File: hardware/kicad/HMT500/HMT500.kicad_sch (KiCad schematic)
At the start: 0 parts

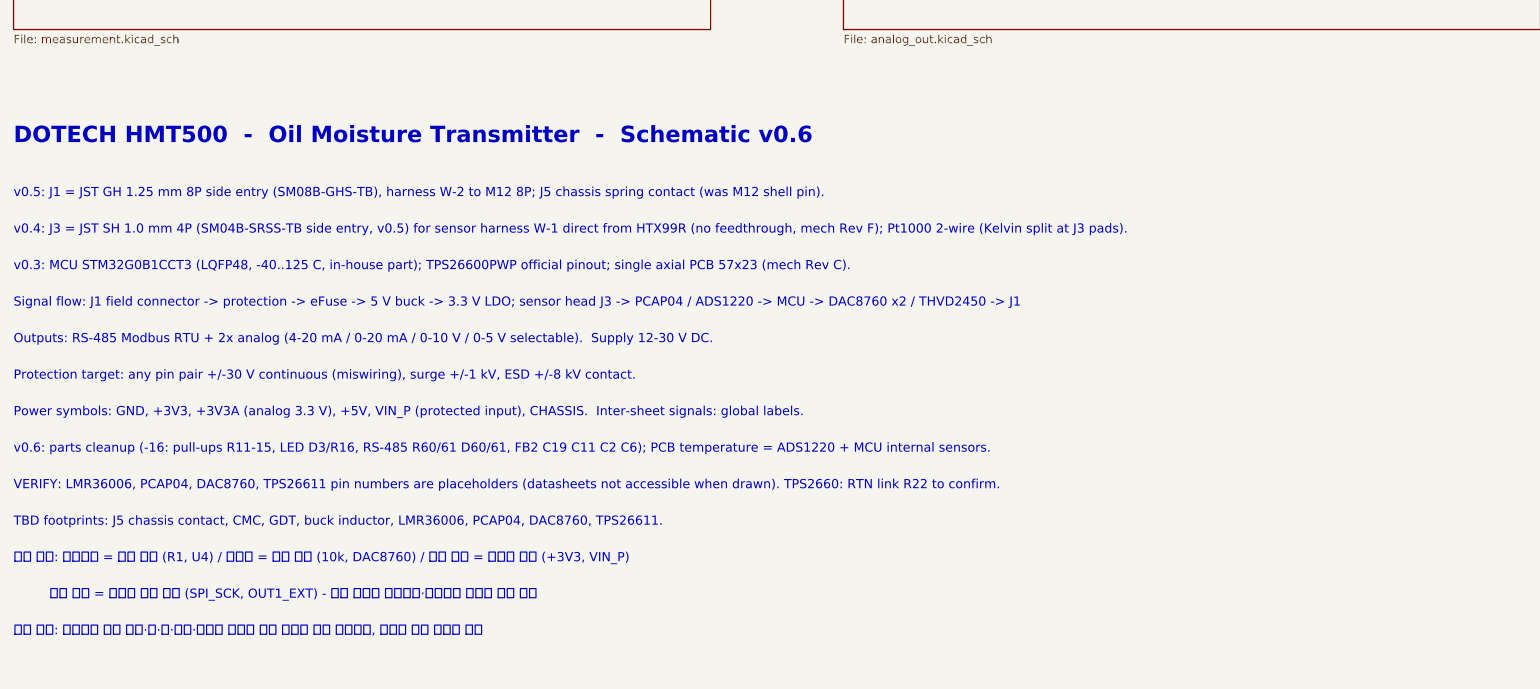
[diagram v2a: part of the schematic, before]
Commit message: Schematic v0.7: DAC8760 real pinout, OPA197 +VSENSE buffer, ISET-R, SPI2 daisy chain
- DAC8760 symbol from datasheet SBAS528D (HTSSOP-24 PWP + EP), same as
  VibrationSensor IVS320; placeholder pins removed, VERIFY flag dropped
- +VSENSE via OPA197 unity-gain follower (U12/U13) of the terminal voltage;
  R31/R41 10k kept as buffer input protection; C45/C55 V+ bypass
- External ISET-R 15k 0.1% 25 ppm (R32/R42)
- DACs on dedicated SPI2 (PB13/14/15) daisy chain with common DAC_LATCH
  (PB10); R33 100k pull-down on DAC_DAISY; ALARM -> PB11/PB3, PWR_FLT -> PB4
- Output protection unification (TPS26611 vs passive) left on hold
- Parts list, circuit-design doc, decision log #24 updated; netlist 70/70, 0 errors

Co-Authored-By: Claude Opus 5.5 <noreply@anthropic.com>
Claude-Session: https://claude.ai/code/session_01JA2o8uJsqp9Vzsg4b665ev
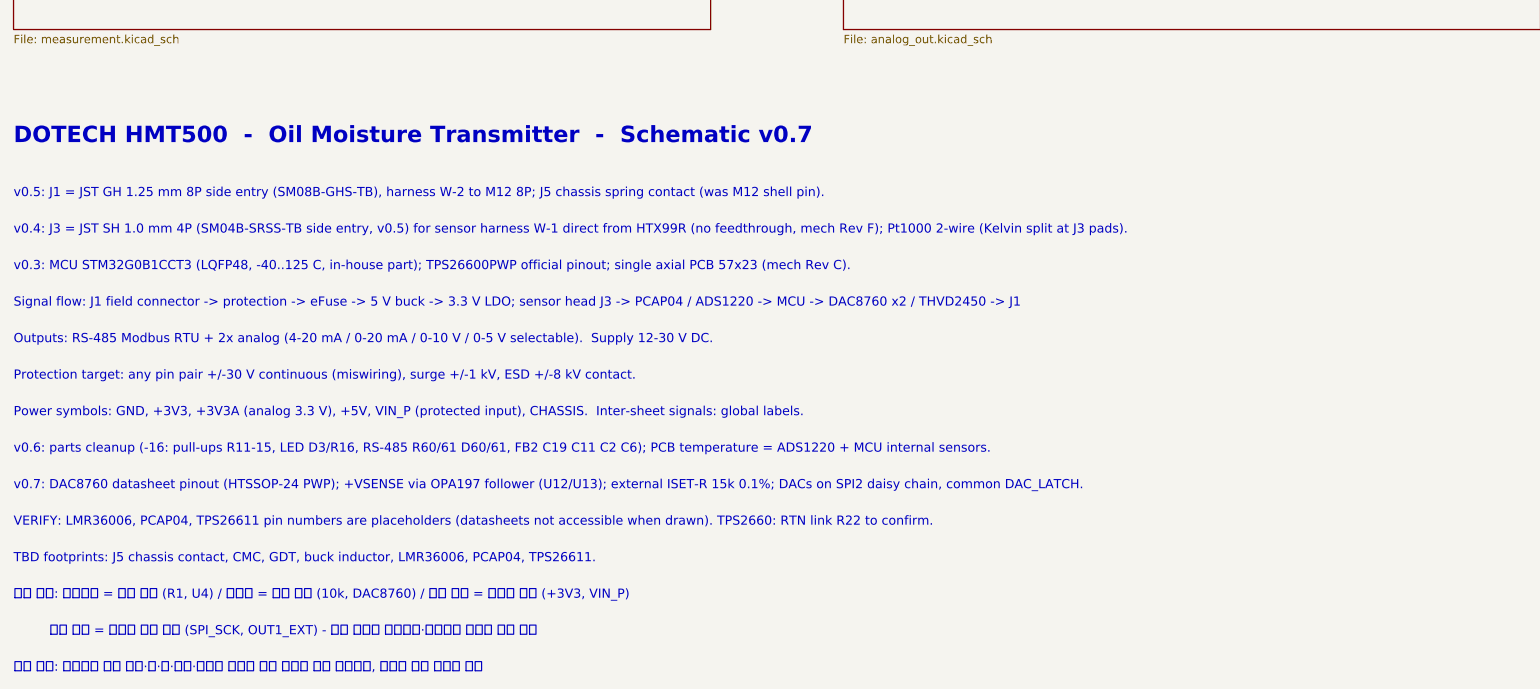
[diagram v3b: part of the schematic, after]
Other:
- note added: "DOTECH HMT500 - Oil Moisture Transmitter - Schematic v0.7"
- note added: "TBD footprints: J5 chassis contact, CMC, GDT, buck inductor, LMR36006, PCAP04, TPS26611."
- note added: "VERIFY: LMR36006, PCAP04, TPS26611 pin numbers are placeholders (datasheets not accessible when drawn). TPS2660: RTN link R22 to confirm."
- note added: "v0.7: DAC8760 datasheet pinout (HTSSOP-24 PWP); +VSENSE via OPA197 follower (U12/U13); external ISET-R 15k 0.1%; DACs on SPI2 daisy chain, common DAC_LATCH."
- note removed: "DOTECH HMT500 - Oil Moisture Transmitter - Schematic v0.6"
- note removed: "TBD footprints: J5 chassis contact, CMC, GDT, buck inductor, LMR36006, PCAP04, DAC8760, TPS26611."
- note removed: "VERIFY: LMR36006, PCAP04, DAC8760, TPS26611 pin numbers are placeholders (datasheets not accessible when drawn). TPS2660: RTN link R22 to confirm."
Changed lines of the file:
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@@
 (kicad_sch (version 20230121) (generator eeschema) (paper "A3")
-(title_block (title "HMT500  Top") (date "2026-09-29") (rev "0.6") (company "DOTECH Co., Ltd.") (comment 1 "Oil moisture transmitter HMT500 - RS-485 + 2x V/I analog output") (comment 2 "Design notes: docs/hw/circuit-design.md") (comment 3 "VERIFY=YES parts: pin numbers LMR36006/PCAP04/DAC8760/TPS26611; TPS2660 R22"))
+(title_block (title "HMT500  Top") (date "2026-09-29") (rev "0.7") (company "DOTECH Co., Ltd.") (comment 1 "Oil moisture transmitter HMT500 - RS-485 + 2x V/I analog output") (comment 2 "Design notes: docs/hw/circuit-design.md") (comment 3 "VERIFY=YES parts: pin numbers LMR36006/PCAP04/TPS26611; TPS2660 R22"))
 (sheet (at 30.48 55.88) (size 106.68 45.72) (fields_autoplaced) (stroke (width 0.1524) (type solid)) (fill (color 0 0 0 0.0000)) (property "Sheetname" "1. Connector & input protection" (at 30.48 55.118 0) (effects (font (size 1.8 1.8) bold) (justify left bottom))) (property "Sheetfile" "connector.kicad_sch" (at 30.48 102.362 0) (effects (font (size 1.27 1.27)) (justify left top))) (instances (project "HMT500" (path "/1ebb025b-11bd-5f7c-aaab-41e2a750e8b3" (page "2")))))
 (text "Field connector, 2-stage bidirectional TVS surge protection, chassis isolation" (at 33.02 78.74 0) (effects (font (size 1.4 1.4)) (justify left bottom)))
@@
 (sheet (at 284.48 132.08) (size 106.68 45.72) (fields_autoplaced) (stroke (width 0.1524) (type solid)) (fill (color 0 0 0 0.0000)) (property "Sheetname" "6. RS-485" (at 284.48 131.318 0) (effects (font (size 1.8 1.8) bold) (justify left bottom))) (property "Sheetfile" "rs485.kicad_sch" (at 284.48 178.562 0) (effects (font (size 1.27 1.27)) (justify left top))) (instances (project "HMT500" (path "/1ebb025b-11bd-5f7c-aaab-41e2a750e8b3" (page "7")))))
 (text "THVD2450 +/-70V fault-protected transceiver" (at 287.02 154.94 0) (effects (font (size 1.4 1.4)) (justify left bottom)))
-(text "DOTECH HMT500  -  Oil Moisture Transmitter  -  Schematic v0.6" (at 30.48 195.58 0) (effects (font (size 2.5 2.5) bold) (justify left bottom)))
+(text "DOTECH HMT500  -  Oil Moisture Transmitter  -  Schematic v0.7" (at 30.48 195.58 0) (effects (font (size 2.5 2.5) bold) (justify left bottom)))
 (text "v0.5: J1 = JST GH 1.25 mm 8P side entry (SM08B-GHS-TB), harness W-2 to M12 8P; J5 chassis spring contact (was M12 shell pin)." (at 30.48 203.708 0) (effects (font (size 1.4 1.4)) (justify left bottom)))
 (text "v0.4: J3 = JST SH 1.0 mm 4P (SM04B-SRSS-TB side entry, v0.5) for sensor harness W-1 direct from HTX99R (no feedthrough, mech Rev F); Pt1000 2-wire (Kelvin split at J3 pads)." (at 30.48 209.296 0) (effects (font (size 1.4 1.4)) (justify left bottom)))
@@
 (text "Power symbols: GND, +3V3, +3V3A (analog 3.3 V), +5V, VIN_P (protected input), CHASSIS.  Inter-sheet signals: global labels." (at 30.48 237.236 0) (effects (font (size 1.4 1.4)) (justify left bottom)))
 (text "v0.6: parts cleanup (-16: pull-ups R11-15, LED D3/R16, RS-485 R60/61 D60/61, FB2 C19 C11 C2 C6); PCB temperature = ADS1220 + MCU internal sensors." (at 30.48 242.824 0) (effects (font (size 1.4 1.4)) (justify left bottom)))
-(text "VERIFY: LMR36006, PCAP04, DAC8760, TPS26611 pin numbers are placeholders (datasheets not accessible when drawn). TPS2660: RTN link R22 to confirm." (at 30.48 248.412 0) (effects (font (size 1.4 1.4)) (justify left bottom)))
-(text "TBD footprints: J5 chassis contact, CMC, GDT, buck inductor, LMR36006, PCAP04, DAC8760, TPS26611." (at 30.48 254 0) (effects (font (size 1.4 1.4)) (justify left bottom)))
-(text "표기 규칙: 부품번호 = 굵은 글자 (R1, U4) / 부품값 = 보통 글자 (10k, DAC8760) / 전원 네트 = 기울인 글자 (+3V3, VIN_P)" (at 30.48 259.588 0) (effects (font (face "NanumGothic") (size 1.4 1.4)) (justify left bottom)))
-(text "         신호 네트 = 테두리 있는 라벨 (SPI_SCK, OUT1_EXT) - 네트 이름은 부품번호·부품명과 겹치지 않게 지음" (at 30.48 265.176 0) (effects (font (face "NanumGothic") (size 1.4 1.4)) (justify left bottom)))
-(text "글자 겹침: 생성기가 부품 몸체·핀·선·라벨·메모와 겹치지 않는 자리에 자동 배치하고, 겹치면 생성 실패로 처리" (at 30.48 270.764 0) (effects (font (face "NanumGothic") (size 1.4 1.4)) (justify left bottom)))
+(text "v0.7: DAC8760 datasheet pinout (HTSSOP-24 PWP); +VSENSE via OPA197 follower (U12/U13); external ISET-R 15k 0.1%; DACs on SPI2 daisy chain, common DAC_LATCH." (at 30.48 248.412 0) (effects (font (size 1.4 1.4)) (justify left bottom)))
+(text "VERIFY: LMR36006, PCAP04, TPS26611 pin numbers are placeholders (datasheets not accessible when drawn). TPS2660: RTN link R22 to confirm." (at 30.48 254 0) (effects (font (size 1.4 1.4)) (justify left bottom)))
+(text "TBD footprints: J5 chassis contact, CMC, GDT, buck inductor, LMR36006, PCAP04, TPS26611." (at 30.48 259.588 0) (effects (font (size 1.4 1.4)) (justify left bottom)))
+(text "표기 규칙: 부품번호 = 굵은 글자 (R1, U4) / 부품값 = 보통 글자 (10k, DAC8760) / 전원 네트 = 기울인 글자 (+3V3, VIN_P)" (at 30.48 265.176 0) (effects (font (face "NanumGothic") (size 1.4 1.4)) (justify left bottom)))
+(text "         신호 네트 = 테두리 있는 라벨 (SPI_SCK, OUT1_EXT) - 네트 이름은 부품번호·부품명과 겹치지 않게 지음" (at 30.48 270.764 0) (effects (font (face "NanumGothic") (size 1.4 1.4)) (justify left bottom)))
+(text "글자 겹침: 생성기가 부품 몸체·핀·선·라벨·메모와 겹치지 않는 자리에 자동 배치하고, 겹치면 생성 실패로 처리" (at 30.48 276.352 0) (effects (font (face "NanumGothic") (size 1.4 1.4)) (justify left bottom)))
 (sheet_instances (path "/" (page "1")))
 )
